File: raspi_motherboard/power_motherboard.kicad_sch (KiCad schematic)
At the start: 19 parts, among them J1 GPIO, J2 Conn_02x04_Top_Bottom

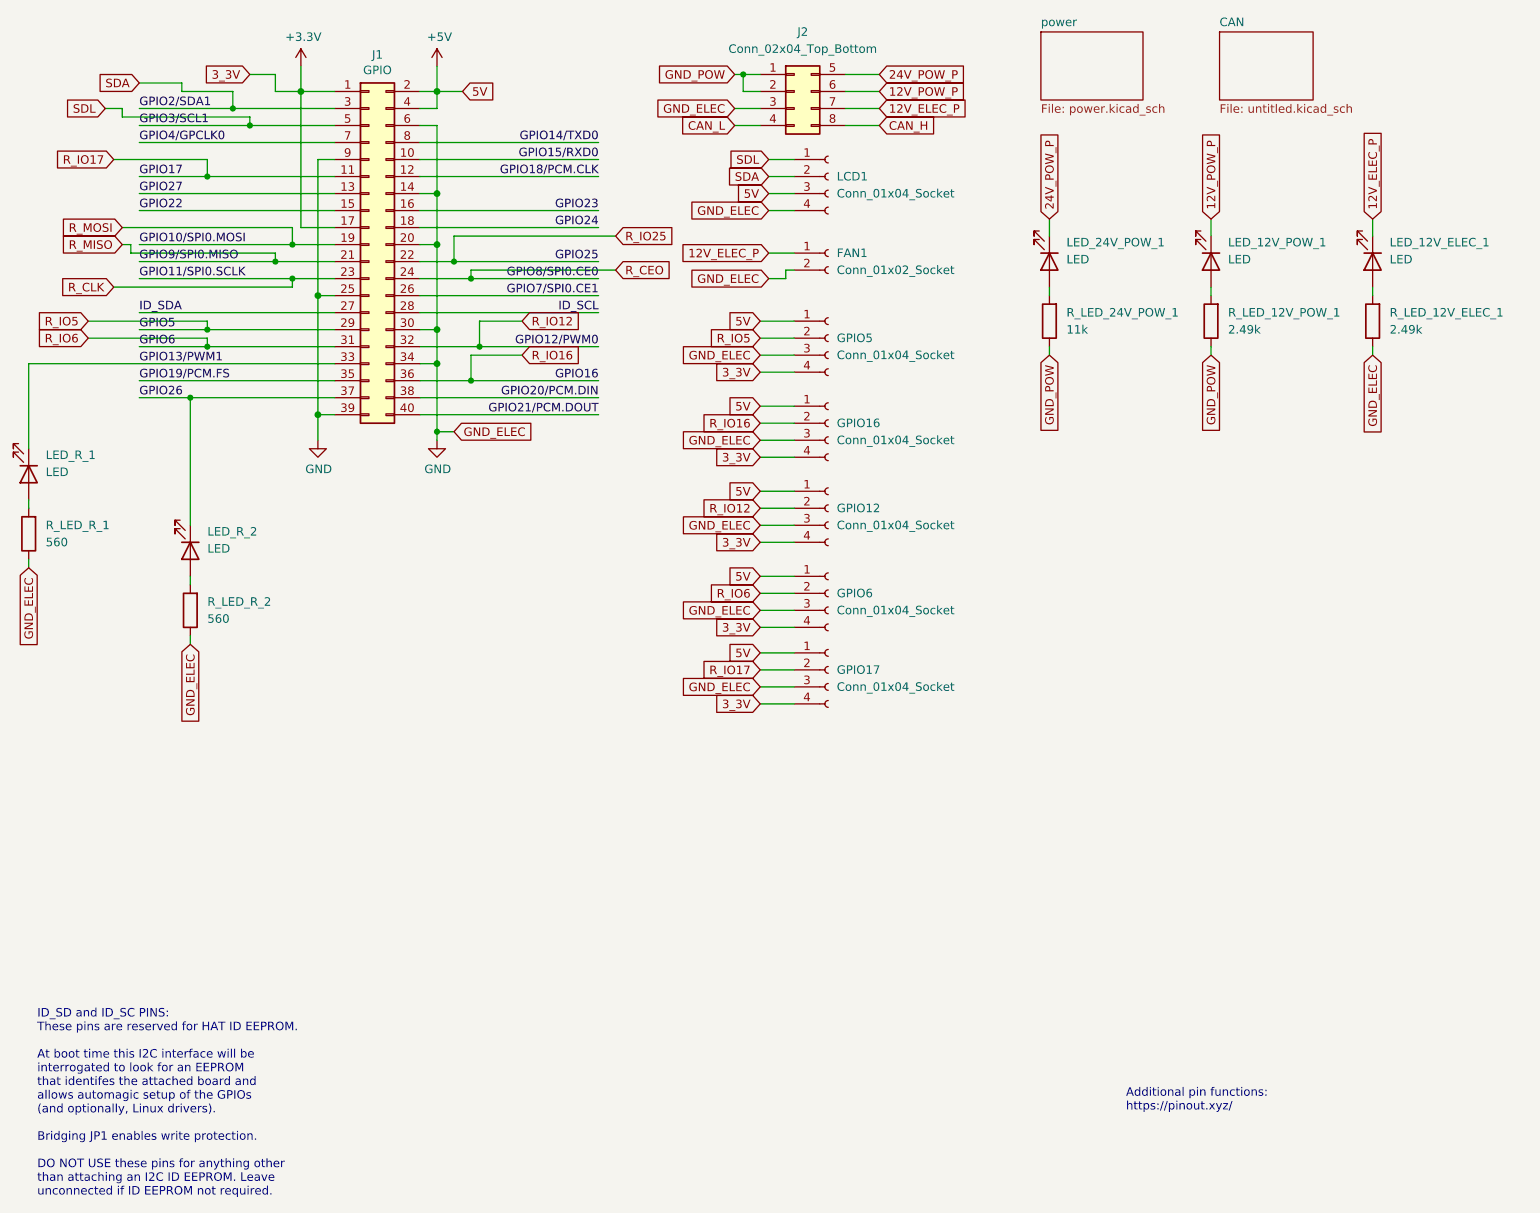
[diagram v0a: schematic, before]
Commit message: V2 of the board: 24 Volt power
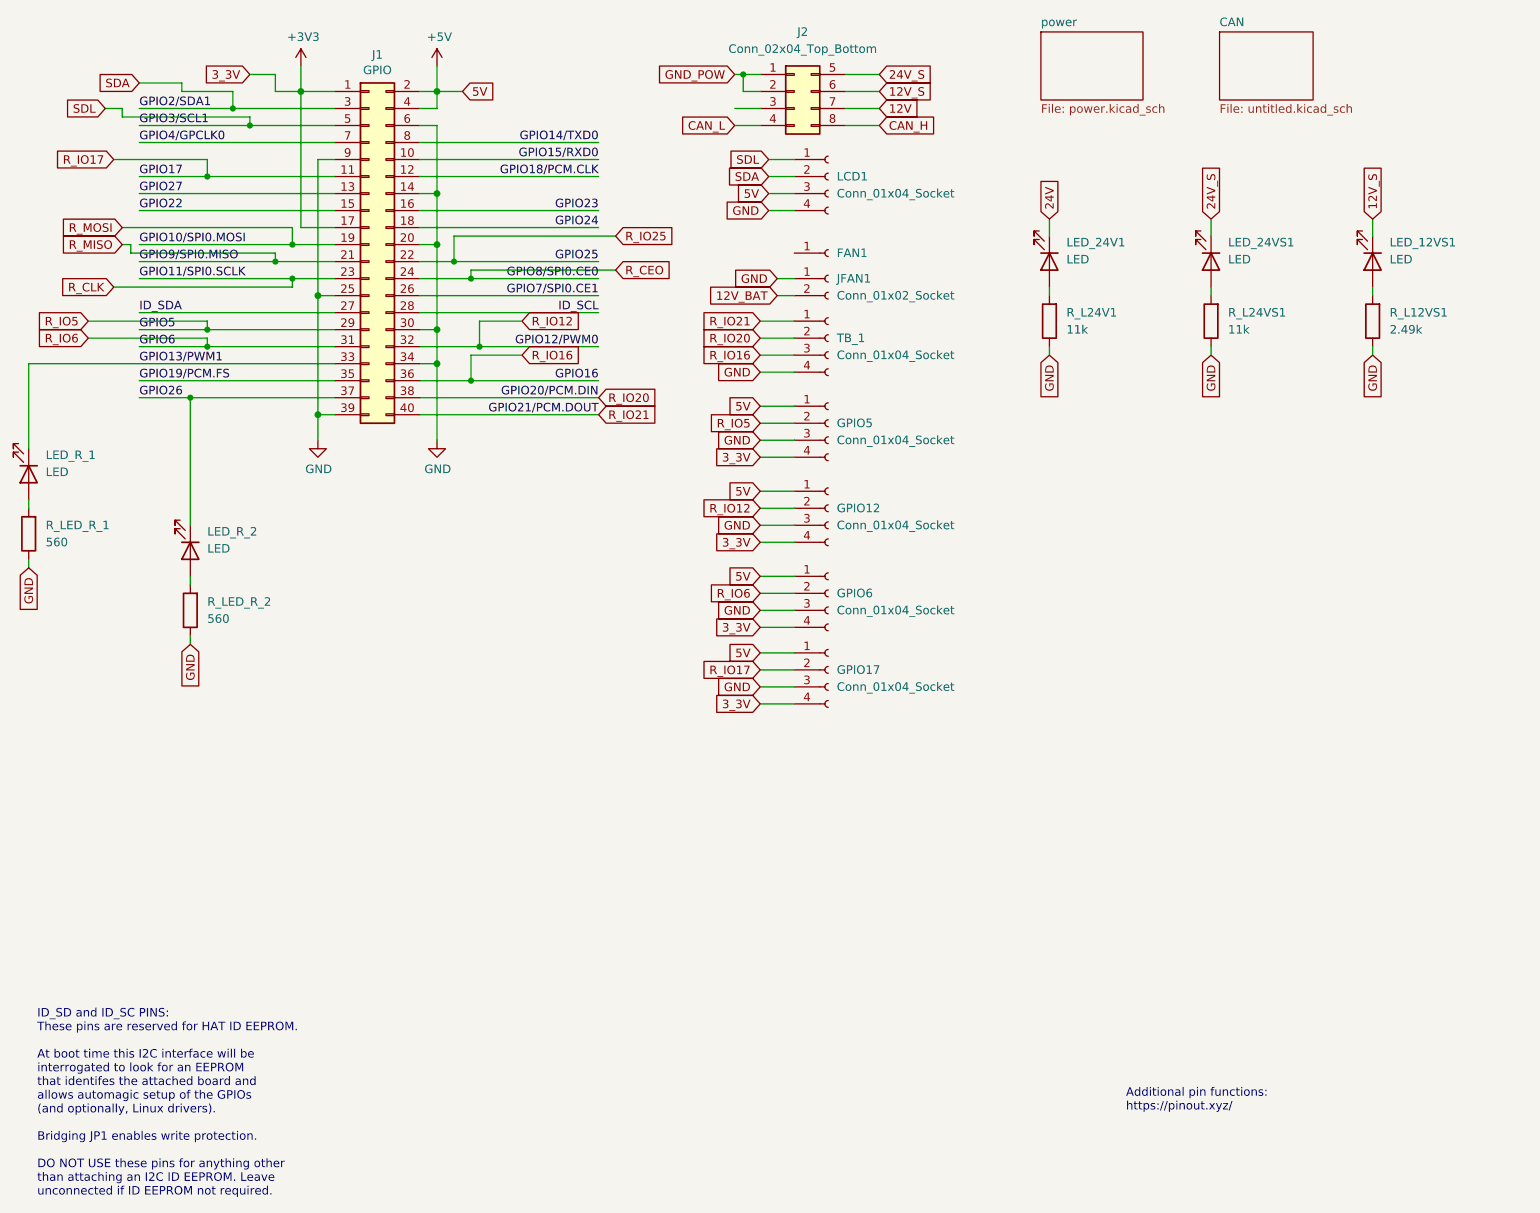
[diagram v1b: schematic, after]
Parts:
- added JFAN1: Conn_01x02_Socket, Connector_PinHeader_1.27mm:PinHeader_1x02_P1.27mm_Vertical, symbol Connector:Conn_01x02_Socket
- R_L24VS1: renamed from R_LED_12V_POW_1; value 2.49k -> 11k
- renumbered GPIO16 to GPIO5, LED_12V_ELEC_1 to LED_12VS1, LED_24V_POW_1 to LED_24V1, LED_12V_POW_1 to LED_24VS1, R_LED_12V_ELEC_1 to R_L12VS1, R_LED_24V_POW_1 to R_L24V1, GPIO5 to TB_1
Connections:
- net +3V3: no longer TB_1.4 (Pin_4)
- net +5V: no longer TB_1.1 (Pin_1)
- net GND: now also R_L24V1.1, R_L24VS1.1, TB_1.4 (Pin_4), JFAN1.1 (Pin_1); no longer FAN1.2 (Pin_2), J2.3 (Pin_3), TB_1.3 (Pin_3)
- net GND_POW: no longer R_L24V1.1, R_L24VS1.1
- net R_IO16: now also TB_1.3 (Pin_3); no longer GPIO5.2 (Pin_2)
- net R_IO5: now also GPIO5.2 (Pin_2); no longer TB_1.2 (Pin_2)
- removed net 12V_ELEC_P: FAN1.1 (Pin_1), J2.7 (Pin_7), LED_12VS1.1 (K)
- net 12V_POW_P renamed 12V_S
- net 12V_S: now also LED_12VS1.1 (K); no longer LED_24VS1.1 (K)
- net 24V_POW_P renamed 24V
- net 24V: no longer J2.5 (Pin_5)
- net GPIO20/PCM.DIN renamed R_IO20
- net R_IO20: now also TB_1.2 (Pin_2)
- net GPIO21/PCM.DOUT renamed R_IO21
- net R_IO21: now also TB_1.1 (Pin_1)
- new net 12V: J2.7 (Pin_7)
- new net 12V_BAT: JFAN1.2 (Pin_2)
- new net 24V_S: J2.5 (Pin_5), LED_24VS1.1 (K)

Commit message: Routed
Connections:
- net 12V_BAT is gone; now on net 12V: JFAN1.2 (Pin_2)
- net GND_POW is gone; now on net GND: J2.1 (Pin_1), J2.2 (Pin_2)
- net GND: now also FAN1.1 (Pin_1)
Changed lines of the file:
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@@
+	)
+	(junction
+		(at 128.27 55.88)
+		(diameter 0)
+		(color 0 0 0 0)
 	)
 	(junction
@@
 	(wire
 		(pts
+			(xy 128.27 52.07) (xy 129.54 52.07)
+		)
+		(stroke
+			(width 0)
+			(type default)
+		)
+	)
+	(wire
+		(pts
 			(xy 124.46 100.33) (xy 129.54 100.33)
 		)
@@
 	(wire
 		(pts
+			(xy 128.27 55.88) (xy 128.27 52.07)
+		)
+		(stroke
+			(width 0)
+			(type default)
+		)
+	)
+	(wire
+		(pts
 			(xy 31.75 45.72) (xy 60.96 45.72)
 		)
@@
 	(wire
 		(pts
+			(xy 128.27 55.88) (xy 129.54 55.88)
+		)
+		(stroke
+			(width 0)
+			(type default)
+		)
+	)
+	(wire
+		(pts
 			(xy 121.92 25.4) (xy 124.46 25.4)
 		)
@@
 	(wire
 		(pts
-			(xy 127 55.88) (xy 129.54 55.88)
+			(xy 127 55.88) (xy 128.27 55.88)
 		)
 		(stroke
@@
 		)
 	)
-	(global_label "12V_BAT"
+	(global_label "12V"
 		(shape input)
 		(at 127 58.42 180)
@@
 		)
 		(property "Intersheetrefs" "${INTERSHEET_REFS}"
-			(at 116.1183 58.42 0)
+			(at 120.4121 58.42 0)
 			(effects
 				(font
@@
 		)
 	)
-	(global_label "GND_POW"
+	(global_label "GND"
 		(shape input)
 		(at 120.65 25.4 180)
@@
 		)
 		(property "Intersheetrefs" "${INTERSHEET_REFS}"
-			(at 108.6797 25.4 0)
-			(effects
-				(font
+			(at 113.6992 25.4 0)
+			(effects
+				(font

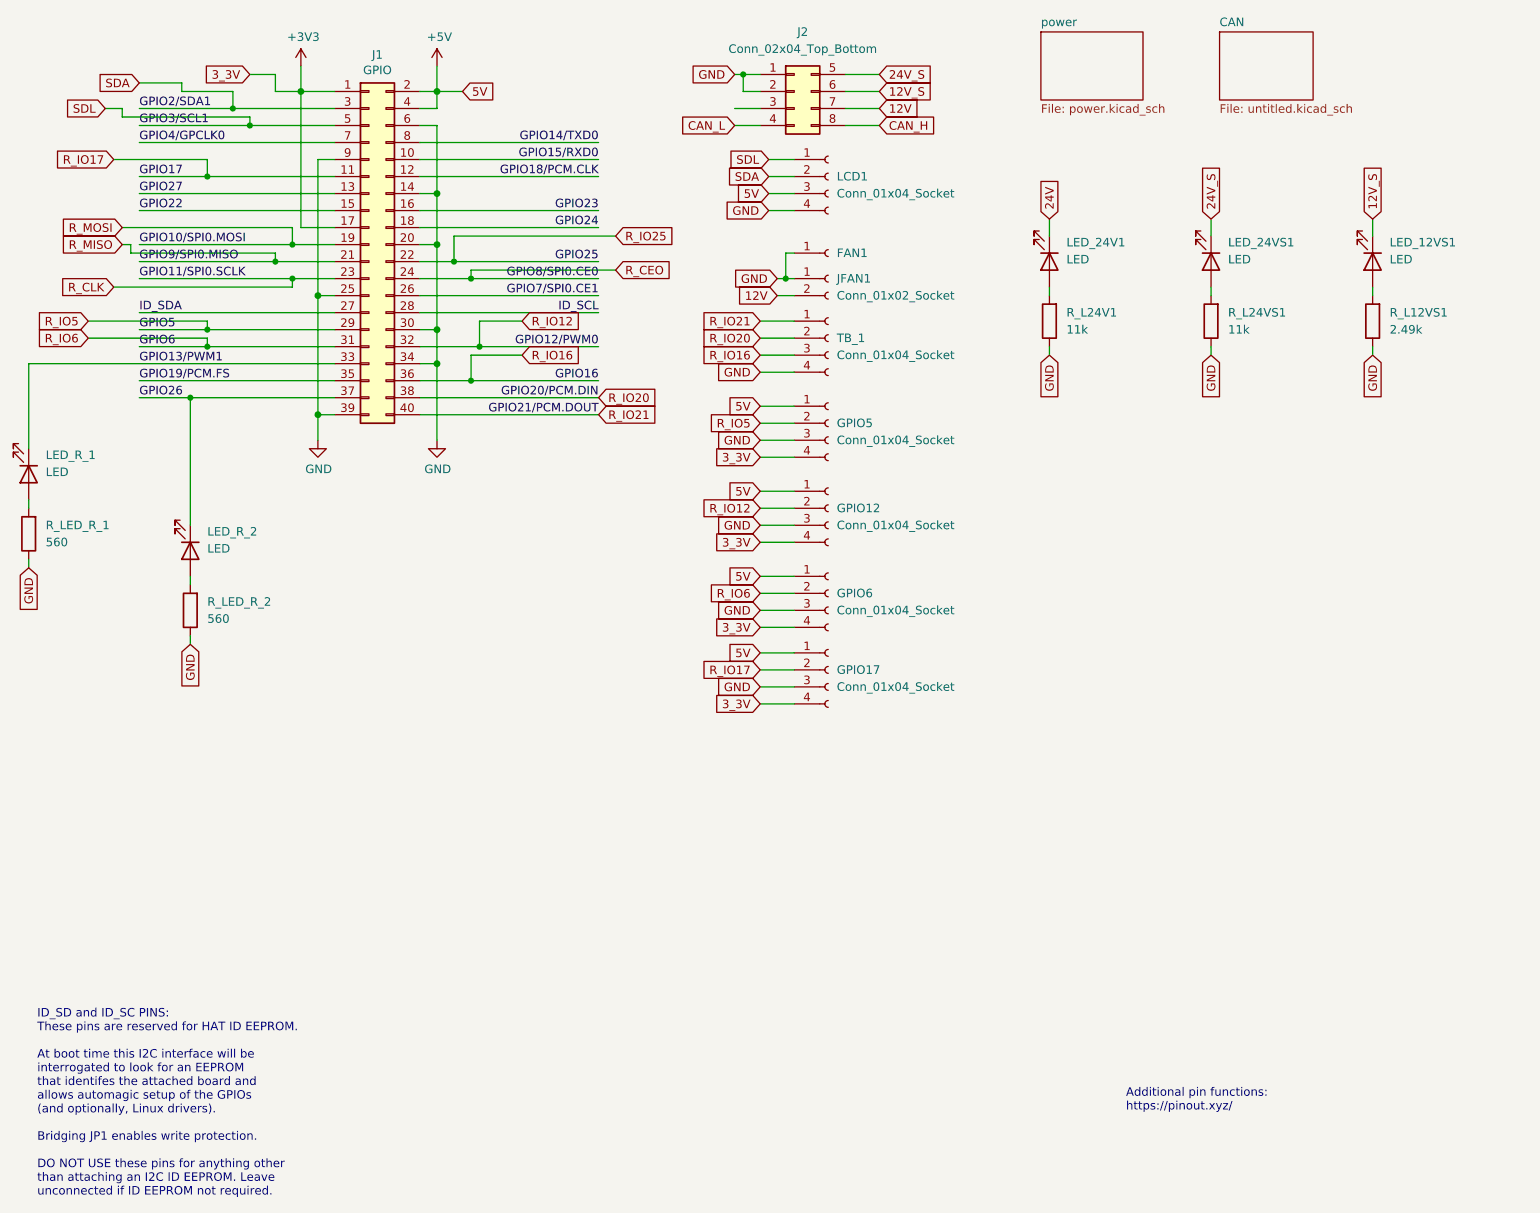
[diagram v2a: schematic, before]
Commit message: Changing connectors
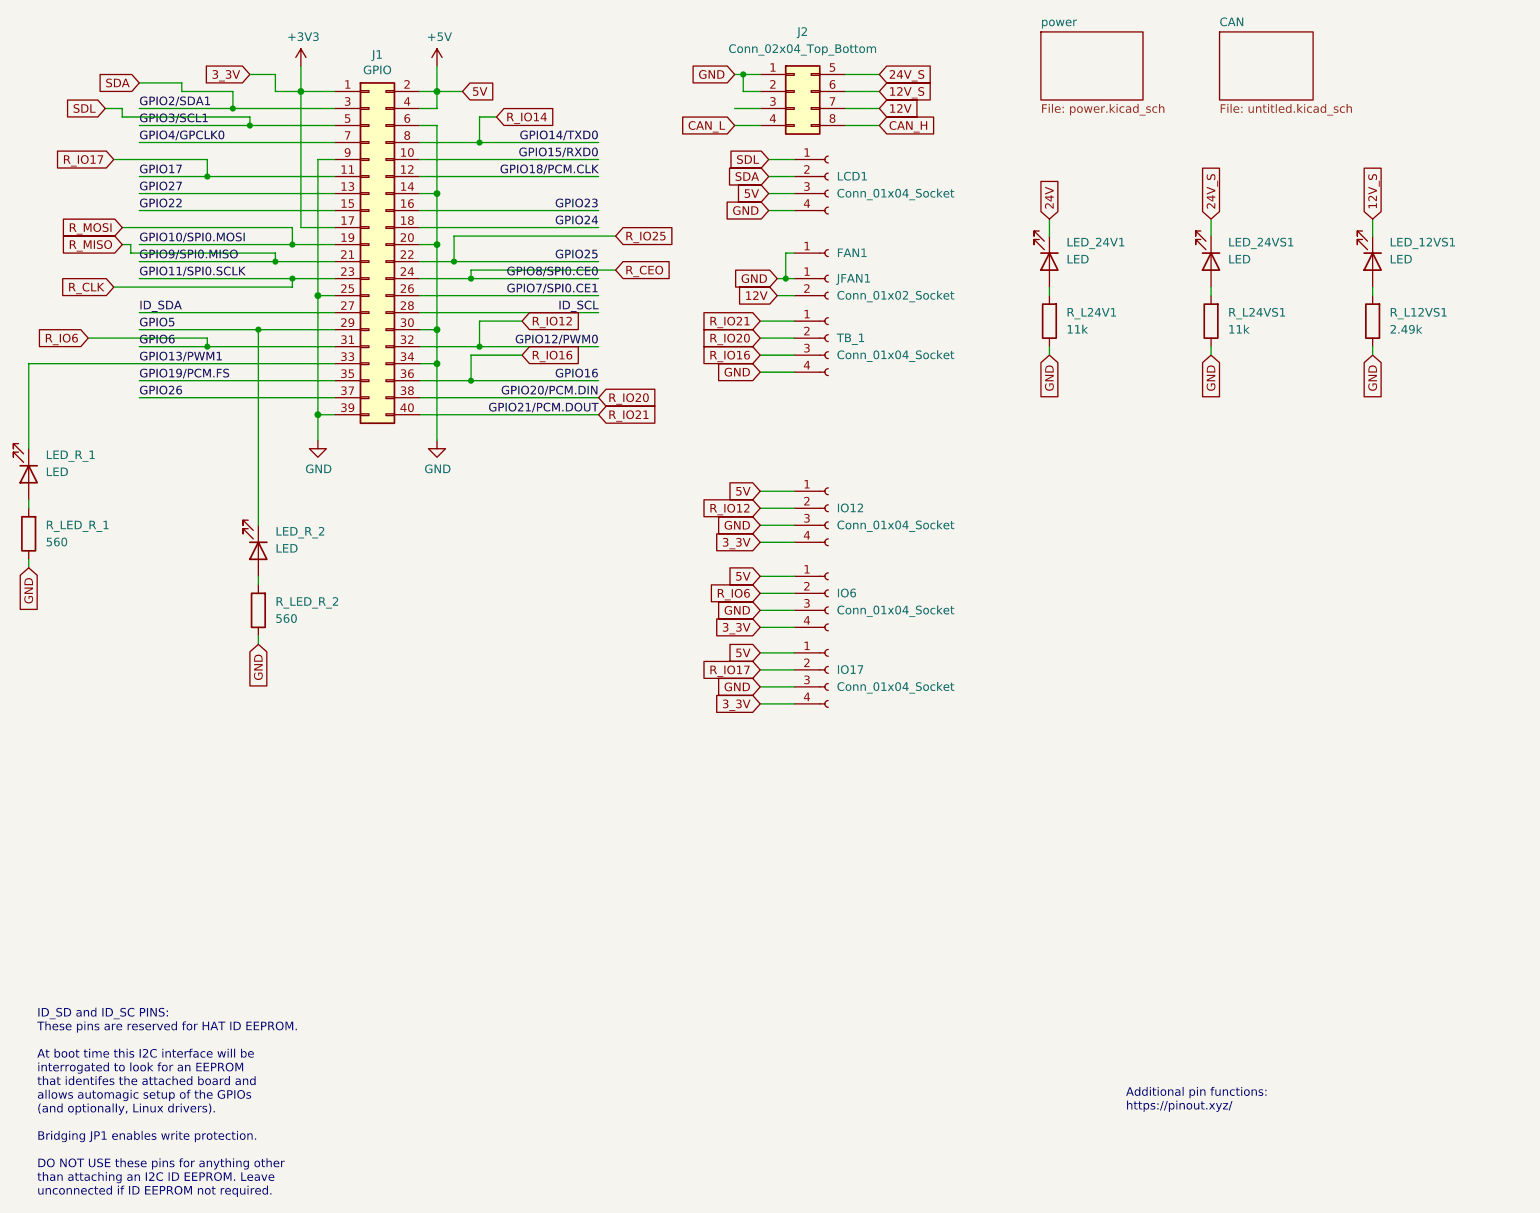
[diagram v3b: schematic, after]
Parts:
- removed GPIO5: Conn_01x04_Socket, Connector_PinSocket_2.54mm:PinSocket_1x04_P2.54mm_Vertical, symbol Connector:Conn_01x04_Socket
- IO12: renamed from GPIO12; footprint Connector_PinSocket_2.54mm:PinSocket_1x04_P2.54mm_Vertical -> Connector_JST:JST_PH_B4B-PH-K_1x04_P2.00mm_Vertical
- IO17: renamed from GPIO17; footprint Connector_PinSocket_2.54mm:PinSocket_1x04_P2.54mm_Vertical -> Connector_JST:JST_PH_B4B-PH-K_1x04_P2.00mm_Vertical
- IO6: renamed from GPIO6; footprint Connector_PinSocket_2.54mm:PinSocket_1x04_P2.54mm_Vertical -> Connector_JST:JST_PH_B4B-PH-K_1x04_P2.00mm_Vertical
- JFAN1: footprint Connector_PinHeader_1.27mm:PinHeader_1x02_P1.27mm_Vertical -> Connector_JST:JST_PH_B2B-PH-K_1x02_P2.00mm_Vertical
- LCD1, TB_1: footprint Connector_PinSocket_2.54mm:PinSocket_1x04_P2.54mm_Vertical -> Connector_JST:JST_PH_B4B-PH-K_1x04_P2.00mm_Vertical
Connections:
- net GPIO26: no longer LED_R_2.1 (K)
- net GPIO14/TXD0 renamed R_IO14
- net R_IO5 renamed GPIO5
- net GPIO5: now also LED_R_2.1 (K)
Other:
- moved on the sheet: LED_R_2, R_LED_R_2

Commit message: Production version
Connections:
- net SDL renamed SCL
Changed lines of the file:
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@@
 		)
 	)
-	(global_label "SDL"
+	(global_label "SCL"
 		(shape input)
 		(at 26.67 30.48 180)
@@
 		)
 	)
-	(global_label "SDL"
+	(global_label "SCL"
 		(shape input)
 		(at 125.73 38.1 180)
